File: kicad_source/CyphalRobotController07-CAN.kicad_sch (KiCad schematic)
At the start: 20 parts, among them J1 BM04B-SRSS-TB, J15 PinHeader_1x04, J16 PinHeader_1x04, J17 PinHeader_1x05, J2 RASPBERRYPI_PICO, J3 BM04B-SRSS-TB, J4 B3B-PH-SM4-TB, SW1 PTS636 SM43 SMTR LFS, U1 24LC64-I/SN

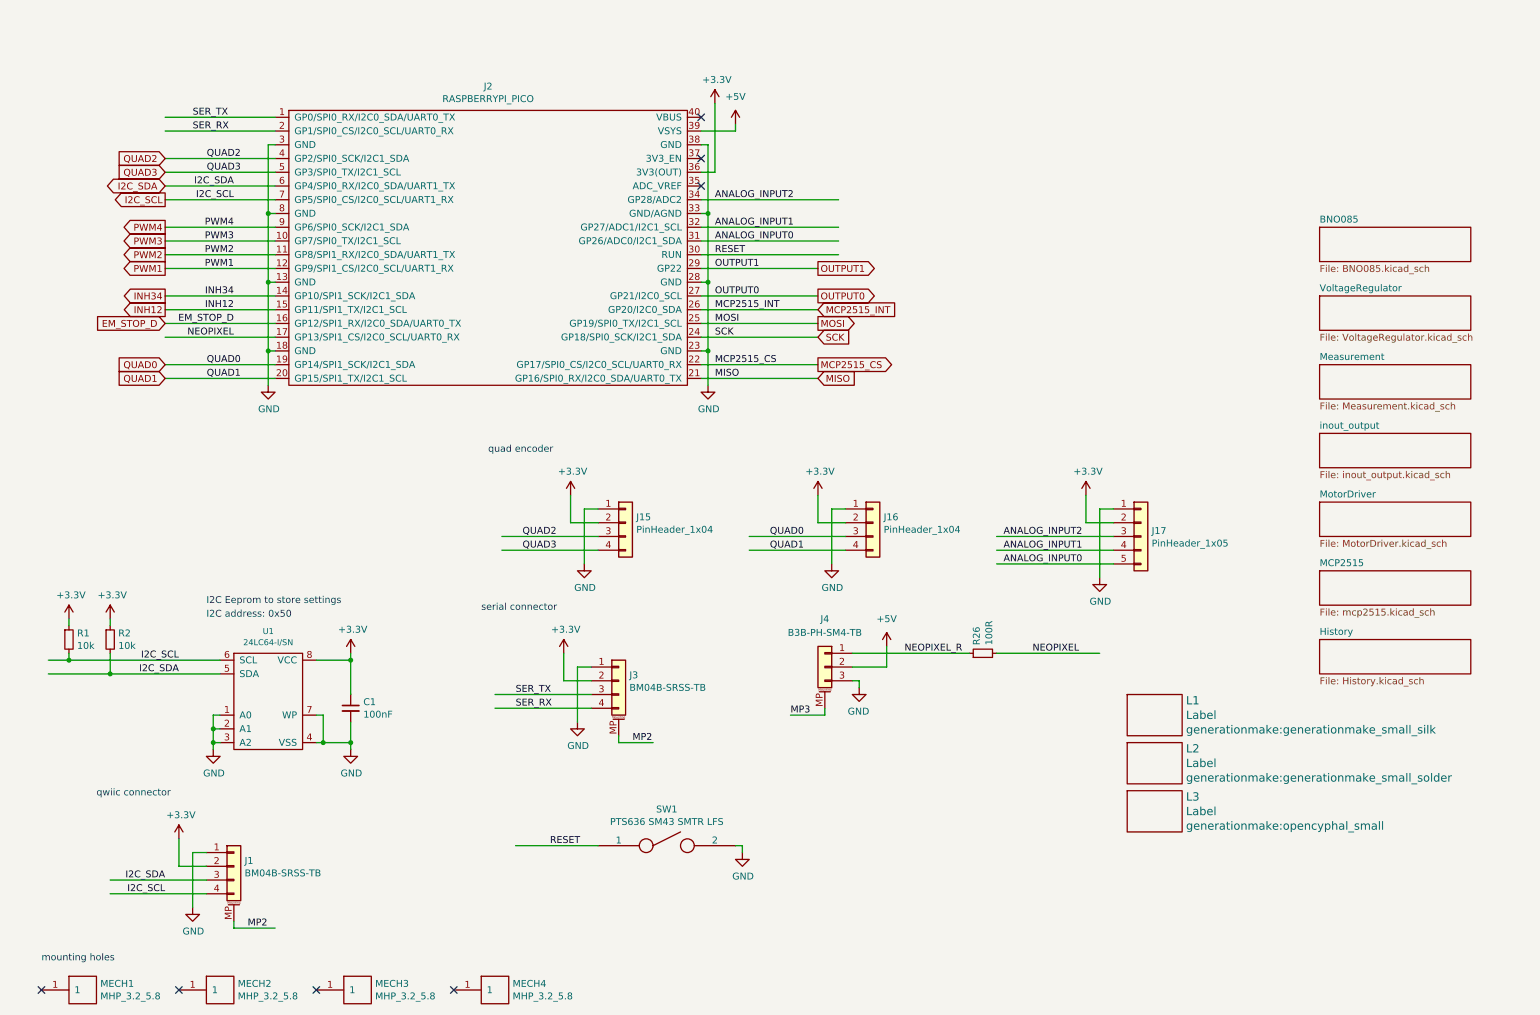
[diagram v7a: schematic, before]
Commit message: added level converters on encoder inputs
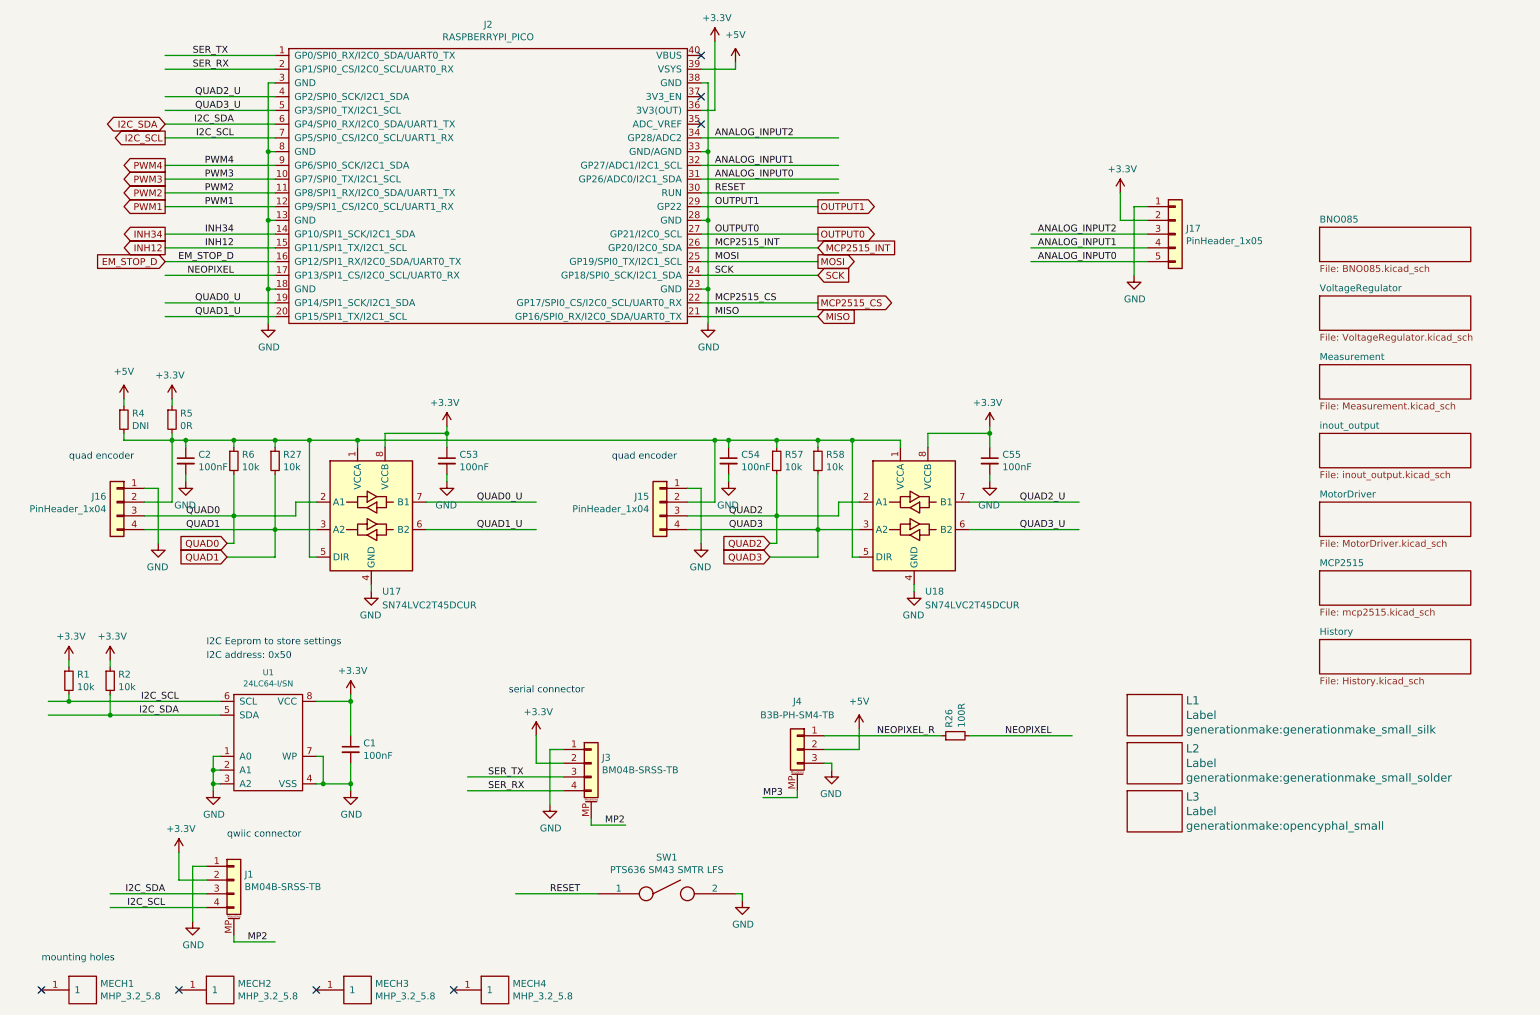
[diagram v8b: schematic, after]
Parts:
- added C2, C53, C54, C55: 100nF, Capacitor_SMD:C_0603_1608Metric, symbol Device:C_Small
- added R27, R57, R58, R6: 10k, Resistor_SMD:R_0603_1608Metric, symbol Device:R_Small
- added R4: DNI, Resistor_SMD:R_0603_1608Metric, symbol Device:R_Small
- added R5: 0R, Resistor_SMD:R_0603_1608Metric, symbol Device:R_Small
- added U17, U18: SN74LVC2T45DCUR, Package_SO:VSSOP-8_2.4x2.1mm_P0.5mm, symbol Logic_LevelTranslator:SN74LVC2T45DCUR
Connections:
- net +3.3V: now also C53.1, C55.1, R5.1, U17.8 (VCCB), U18.8 (VCCB); no longer J15.2 (Pin_2), J16.2 (Pin_2)
- net +5V: now also R4.1
- net GND: now also C2.2, C53.2, C54.2, C55.2, U17.4 (GND), U18.4 (GND)
- net QUAD0: now also R6.2, U17.2 (A1); no longer J2.19 (GP14/SPI1_SCK/I2C1_SDA)
- net QUAD1: now also R27.2, U17.3 (A2); no longer J2.20 (GP15/SPI1_TX/I2C1_SCL)
- net QUAD2: now also R57.2, U18.2 (A1); no longer J2.4 (GP2/SPI0_SCK/I2C1_SDA)
- net QUAD3: now also R58.2, U18.3 (A2); no longer J2.5 (GP3/SPI0_TX/I2C1_SCL)
- new net: C2.1, C54.1, J15.2 (Pin_2), J16.2 (Pin_2), R27.1, R4.2, R5.2, R57.1, R58.1, R6.1, U17.1 (VCCA), U17.5 (DIR), U18.1 (VCCA), U18.5 (DIR)
- new net QUAD0_U: J2.19 (GP14/SPI1_SCK/I2C1_SDA), U17.7 (B1)
- new net QUAD1_U: J2.20 (GP15/SPI1_TX/I2C1_SCL), U17.6 (B2)
- new net QUAD2_U: J2.4 (GP2/SPI0_SCK/I2C1_SDA), U18.7 (B1)
- new net QUAD3_U: J2.5 (GP3/SPI0_TX/I2C1_SCL), U18.6 (B2)
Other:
- moved on the sheet: C1, J1, J16, J17, J2, J3, J4, R1, R2, R26, SW1, U1
